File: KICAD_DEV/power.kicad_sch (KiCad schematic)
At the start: 16 parts, among them J1 USB_C_Receptacle_USB2.0_14P, J2 Screw_Terminal_01x02, U2 USBLC6-2SC6, U3 LMR33640ADDA

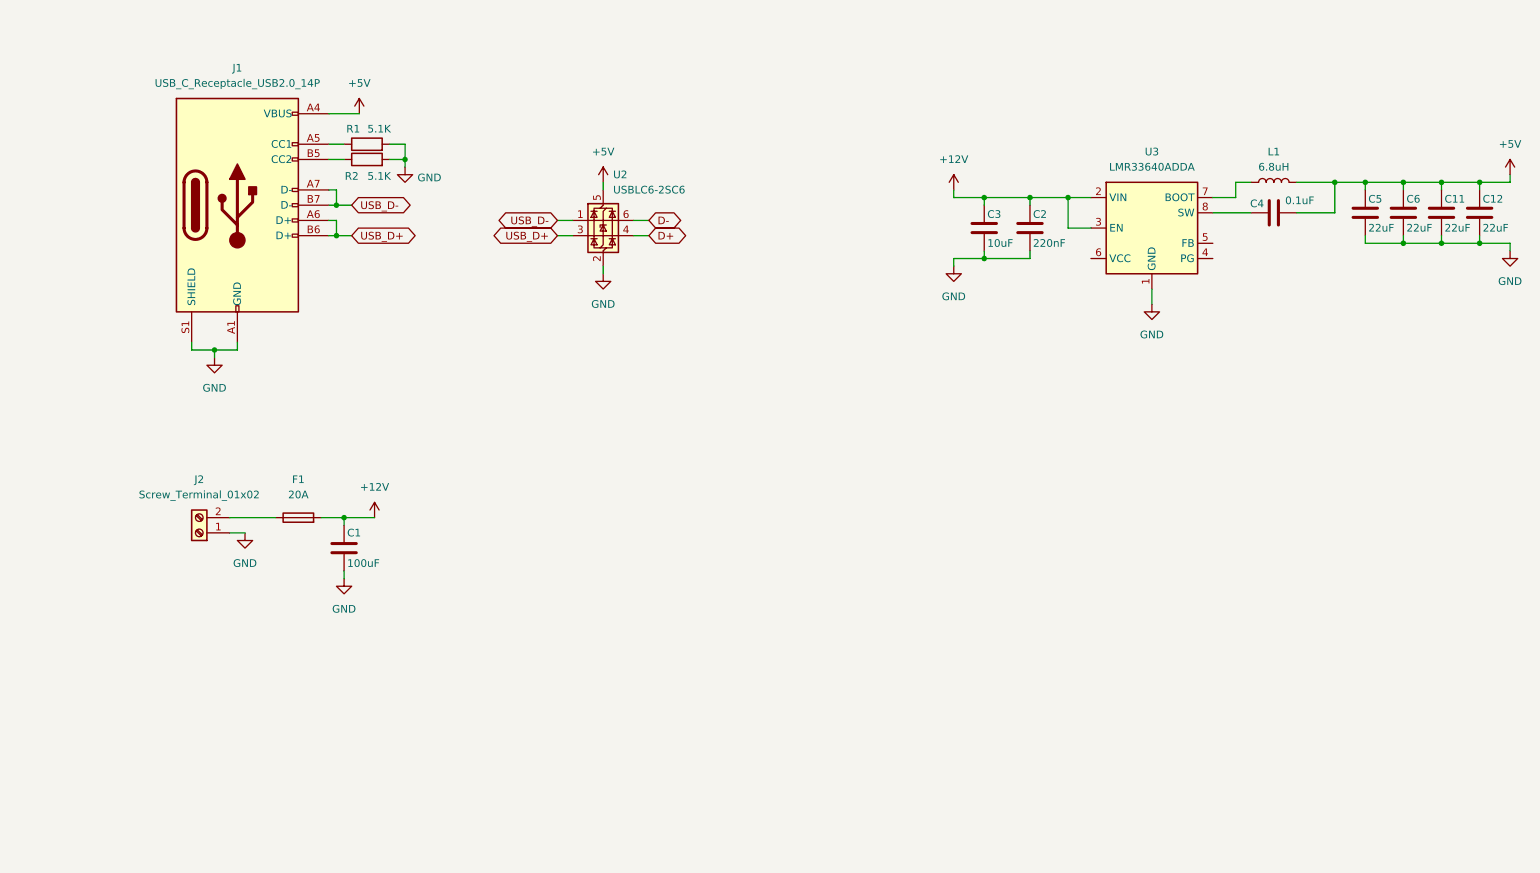
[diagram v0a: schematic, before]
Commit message: finished buck converter wiring!
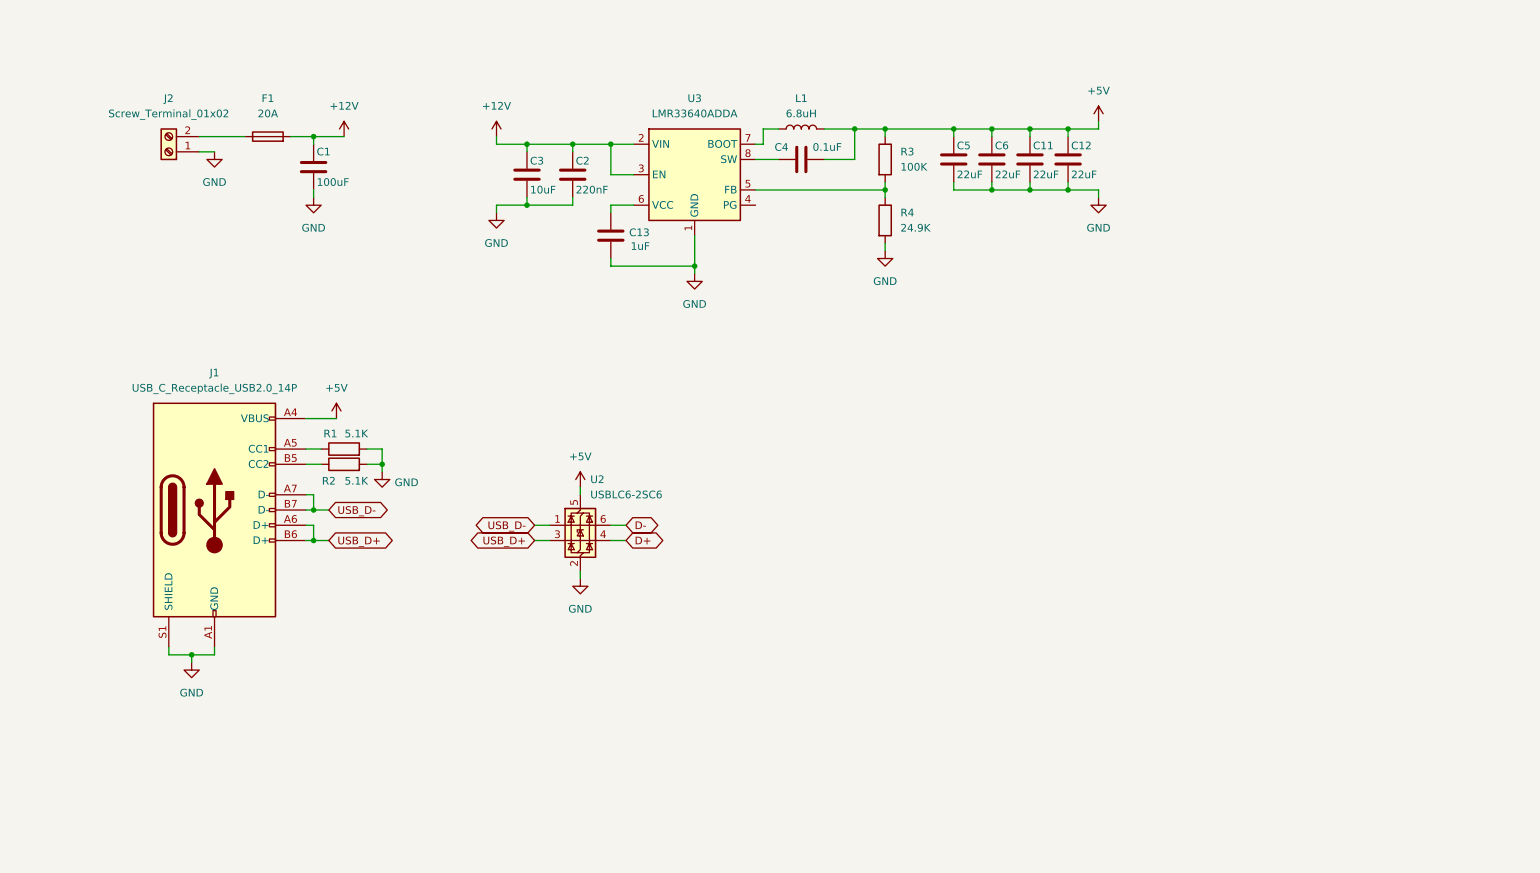
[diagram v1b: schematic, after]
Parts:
- added C13: 1uF, symbol Device:C
- added R3: 100K, symbol Device:R
- added R4: 24.9K, symbol Device:R
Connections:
- net +5V: now also R3.1
- net GND: now also C13.2, R4.2
- net at U3.5 (FB): now also R3.2, R4.1
- net at U3.6 (VCC): now also C13.1
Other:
- moved on the sheet: C1, C11, C12, C2, C3, C4, C5, C6, F1, J1, J2, L1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

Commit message: added all the basic footprints!
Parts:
- C11, C12, C5, C6: footprint (none) -> Capacitor_SMD:C_0805_2012Metric
- C13, C2, C4: footprint (none) -> Capacitor_SMD:C_0402_1005Metric
- C3: footprint (none) -> Capacitor_SMD:C_0603_1608Metric
- R1, R2, R3, R4: footprint (none) -> Resistor_SMD:R_0402_1005Metric
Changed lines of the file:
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@@
 			)
 		)
-		(property "Footprint" ""
+		(property "Footprint" "Resistor_SMD:R_0402_1005Metric"
 			(at 62.23 97.028 90)
 			(effects
@@
 			)
 		)
-		(property "Footprint" ""
+		(property "Footprint" "Capacitor_SMD:C_0805_2012Metric"
 			(at 177.4952 48.26 0)
 			(effects
@@
 			)
 		)
-		(property "Footprint" ""
+		(property "Footprint" "Capacitor_SMD:C_0805_2012Metric"
 			(at 164.7952 48.26 0)
 			(effects
@@
 			)
 		)
-		(property "Footprint" ""
+		(property "Footprint" "Capacitor_SMD:C_0402_1005Metric"
 			(at 142.24 43.4848 0)
 			(effects
@@
 			)
 		)
-		(property "Footprint" ""
+		(property "Footprint" "Capacitor_SMD:C_0805_2012Metric"
 			(at 171.1452 48.26 0)
 			(effects
@@
 			)
 		)
-		(property "Footprint" ""
+		(property "Footprint" "Capacitor_SMD:C_0805_2012Metric"
 			(at 183.8452 48.26 0)
 			(effects
@@
 			)
 		)
-		(property "Footprint" ""
+		(property "Footprint" "Capacitor_SMD:C_0402_1005Metric"
 			(at 107.6452 60.96 0)
 			(effects
@@
 			)
 		)
-		(property "Footprint" ""
+		(property "Footprint" "Capacitor_SMD:C_0603_1608Metric"
 			(at 93.6752 50.8 0)
 			(effects
@@
 			)
 		)
-		(property "Footprint" ""
+		(property "Footprint" "Resistor_SMD:R_0402_1005Metric"
 			(at 62.23 94.488 90)
 			(effects
@@
 			)
 		)
-		(property "Footprint" ""
+		(property "Footprint" "Capacitor_SMD:C_0402_1005Metric"
 			(at 101.2952 50.8 0)
 			(effects
@@
 			)
 		)
-		(property "Footprint" ""
+		(property "Footprint" "Resistor_SMD:R_0402_1005Metric"
 			(at 150.622 54.61 90)
 			(effects
@@
 			)
 		)
-		(property "Footprint" ""
+		(property "Footprint" "Resistor_SMD:R_0402_1005Metric"
 			(at 150.622 44.45 90)
 			(effects

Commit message: assigning more footprints!g
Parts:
- J2: footprint (none) -> TerminalBlock_Phoenix:TerminalBlock_Phoenix_PT-1,5-2-5.0-H_1x02_P5.00mm_Horizontal; Part (none) -> 1935776
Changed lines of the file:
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@@
 		(on_board yes)
 		(dnp no)
-		(fields_autoplaced yes)
 		(property "Reference" "J2"
-			(at 33.02 34.29 0)
+			(at 33.02 30.988 0)
 			(effects
 				(font
@@
 		)
 		(property "Value" "Screw_Terminal_01x02"
-			(at 33.02 36.83 0)
+			(at 33.02 33.528 0)
 			(effects
 				(font
@@
 			)
 		)
-		(property "Footprint" ""
+		(property "Footprint" "TerminalBlock_Phoenix:TerminalBlock_Phoenix_PT-1,5-2-5.0-H_1x02_P5.00mm_Horizontal"
 			(at 33.02 43.18 0)
 			(effects
@@
 			)
 		)
+		(property "Part" "1935776"
+			(at 33.02 36.322 0)
+			(effects
+				(font
+					(size 1.27 1.27)
+				)
+			)
+		)

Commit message: all footprints are in!
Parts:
- C1: footprint (none) -> Capacitor_SMD:C_Elec_8x6.2; Part (none) -> 25SVPF100M
- F1: footprint (none) -> Fuse:Fuse_Blade_Mini_directSolder
- J1: footprint (none) -> kai's library:USB_C_Receptacle_HRO_TYPE-C-31-M-12
- L1: footprint (none) -> Inductor_SMD:L_TechFuse_SL0650; Part (none) -> SMMS0650-6R8M
- U3: Current (none) -> 4A Continuous, 5A Max
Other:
- note added: "Probably change to fuse holder"
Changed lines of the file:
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@@
 	(generator_version "9.0")
 	(paper "A4")
+	(text "Probably change to fuse holder"
+		(exclude_from_sim no)
+		(at 50.546 26.67 0)
+		(effects
+			(font
+				(size 1.27 1.27)
+			)
+		)
+	)
 	(junction
 		(at 182.88 39.37)
@@
 			)
 		)
-		(property "Footprint" ""
+		(property "Footprint" "Fuse:Fuse_Blade_Mini_directSolder"
 			(at 49.53 42.418 90)
 			(effects
@@
 		(on_board yes)
 		(dnp no)
-		(fields_autoplaced yes)
 		(property "Reference" "L1"
-			(at 138.43 34.29 90)
+			(at 138.43 31.242 90)
 			(effects
 				(font
@@
 		)
 		(property "Value" "6.8uH"
-			(at 138.43 36.83 90)
-			(effects
-				(font
-					(size 1.27 1.27)
-				)
-			)
-		)
-		(property "Footprint" ""
+			(at 138.43 33.782 90)
+			(effects
+				(font
+					(size 1.27 1.27)
+				)
+			)
+		)
+		(property "Footprint" "Inductor_SMD:L_TechFuse_SL0650"
 			(at 138.43 39.37 0)
 			(effects
@@
 				)
 				(hide yes)
+			)
+		)
+		(property "Part" "SMMS0650-6R8M"
+			(at 138.43 36.322 90)
+			(effects
+				(font
+					(size 1.27 1.27)
+				)
 			)
 		)
@@
 		(dnp no)
 		(property "Reference" "C1"
-			(at 57.658 43.18 0)
+			(at 60.452 43.434 0)
 			(effects
 				(font
@@
 		)
 		(property "Value" "100uF"
-			(at 57.658 48.26 0)
+			(at 60.452 45.72 0)
 			(effects
 				(font
@@
 			)
 		)
-		(property "Footprint" ""
+		(property "Footprint" "Capacitor_SMD:C_Elec_8x6.2"
 			(at 58.1152 49.53 0)
 			(effects
@@
 				)
 				(hide yes)
+			)
+		)
+		(property "Part" "25SVPF100M"
+			(at 66.802 48.26 0)
+			(effects
+				(font
+					(size 1.27 1.27)
+				)
 			)
 		)
@@
 		(on_board yes)
 		(dnp no)
-		(fields_autoplaced yes)
 		(property "Reference" "U3"
 			(at 120.65 34.29 0)
@@
 				)
 				(hide yes)
+			)
+		)
+		(property "Current" "4A Continuous, 5A Max"
+			(at 120.65 27.432 0)
+			(effects
+				(font
+					(size 1.27 1.27)
+				)
 			)
 		)
@@
 			)
 		)
-		(property "Footprint" ""
+		(property "Footprint" "kai's library:USB_C_Receptacle_HRO_TYPE-C-31-M-12"
 			(at 44.45 102.87 0)
 			(effects

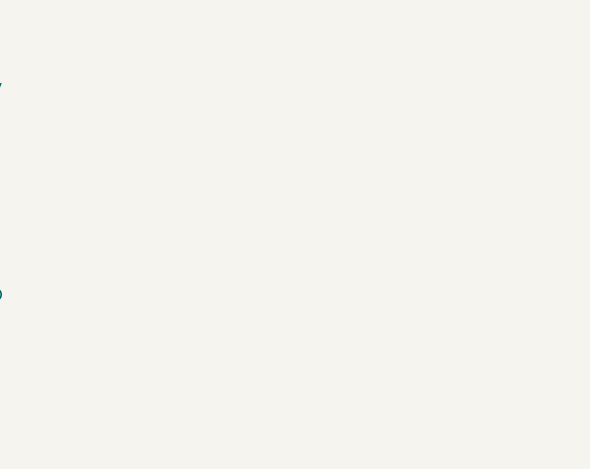
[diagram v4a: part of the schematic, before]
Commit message: added in the 1.5A 3V3 LDO!
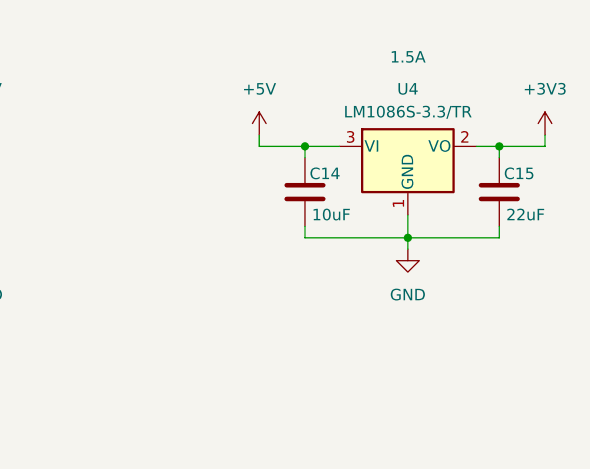
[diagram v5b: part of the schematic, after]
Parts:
- added C14: 10uF, symbol Device:C
- added C15: 22uF, symbol Device:C
- added U4: LM1086S-3.3/TR, Package_TO_SOT_SMD:TO-263-3_TabPin2, symbol Regulator_Linear:LM1084-3.3
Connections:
- net +5V: now also C14.1, U4.3 (VI)
- net GND: now also C14.2, C15.2, U4.1 (GND)
- new net +3V3: C15.1, U4.2 (VO)

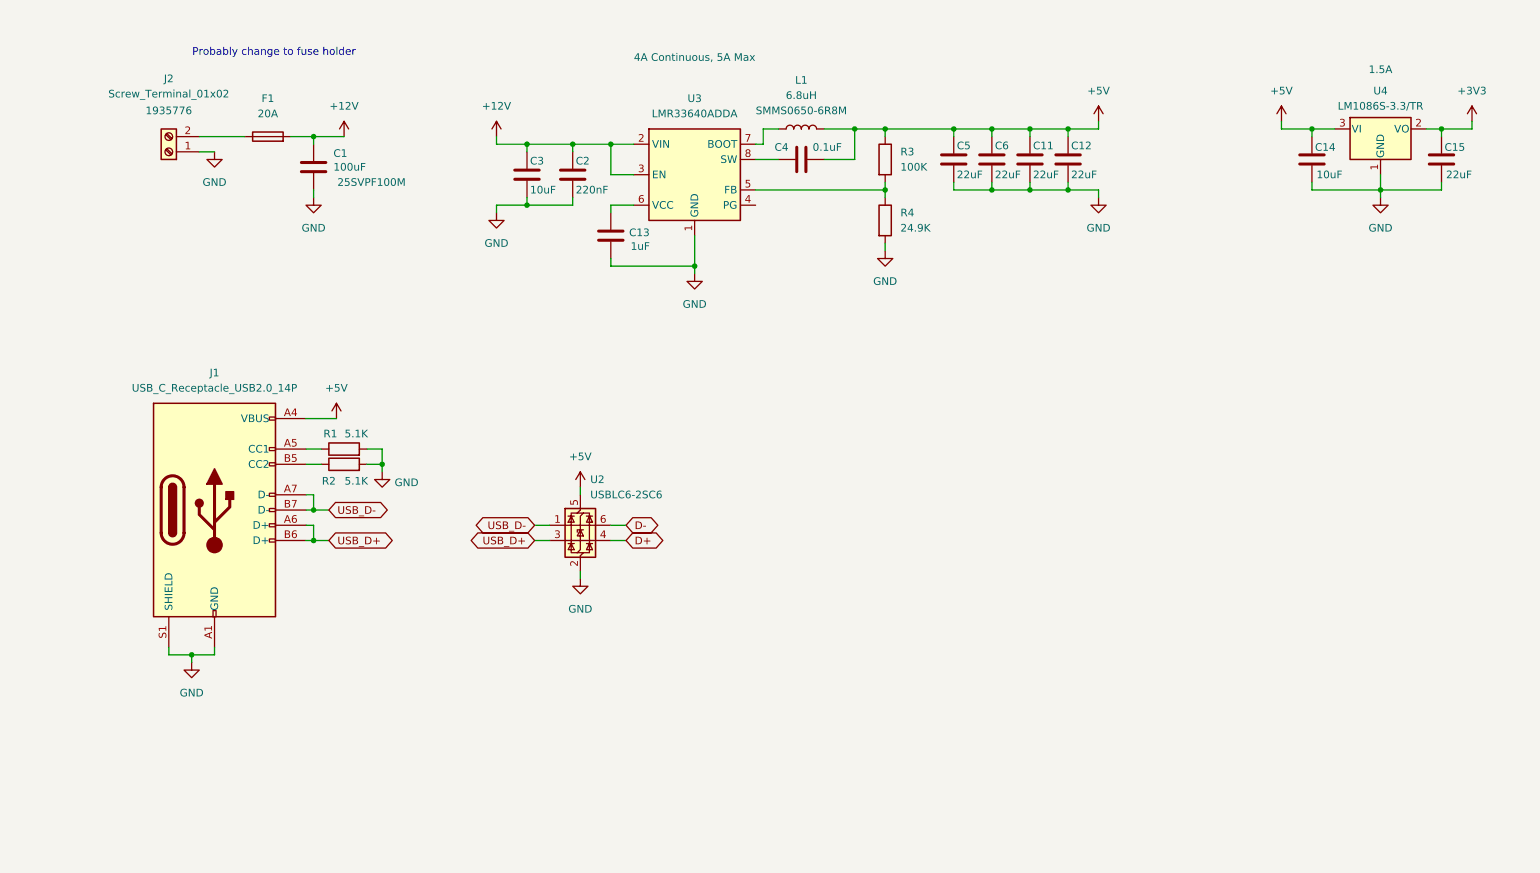
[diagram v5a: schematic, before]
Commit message: cleaning up the schematic, adding some footnotes for contributors!
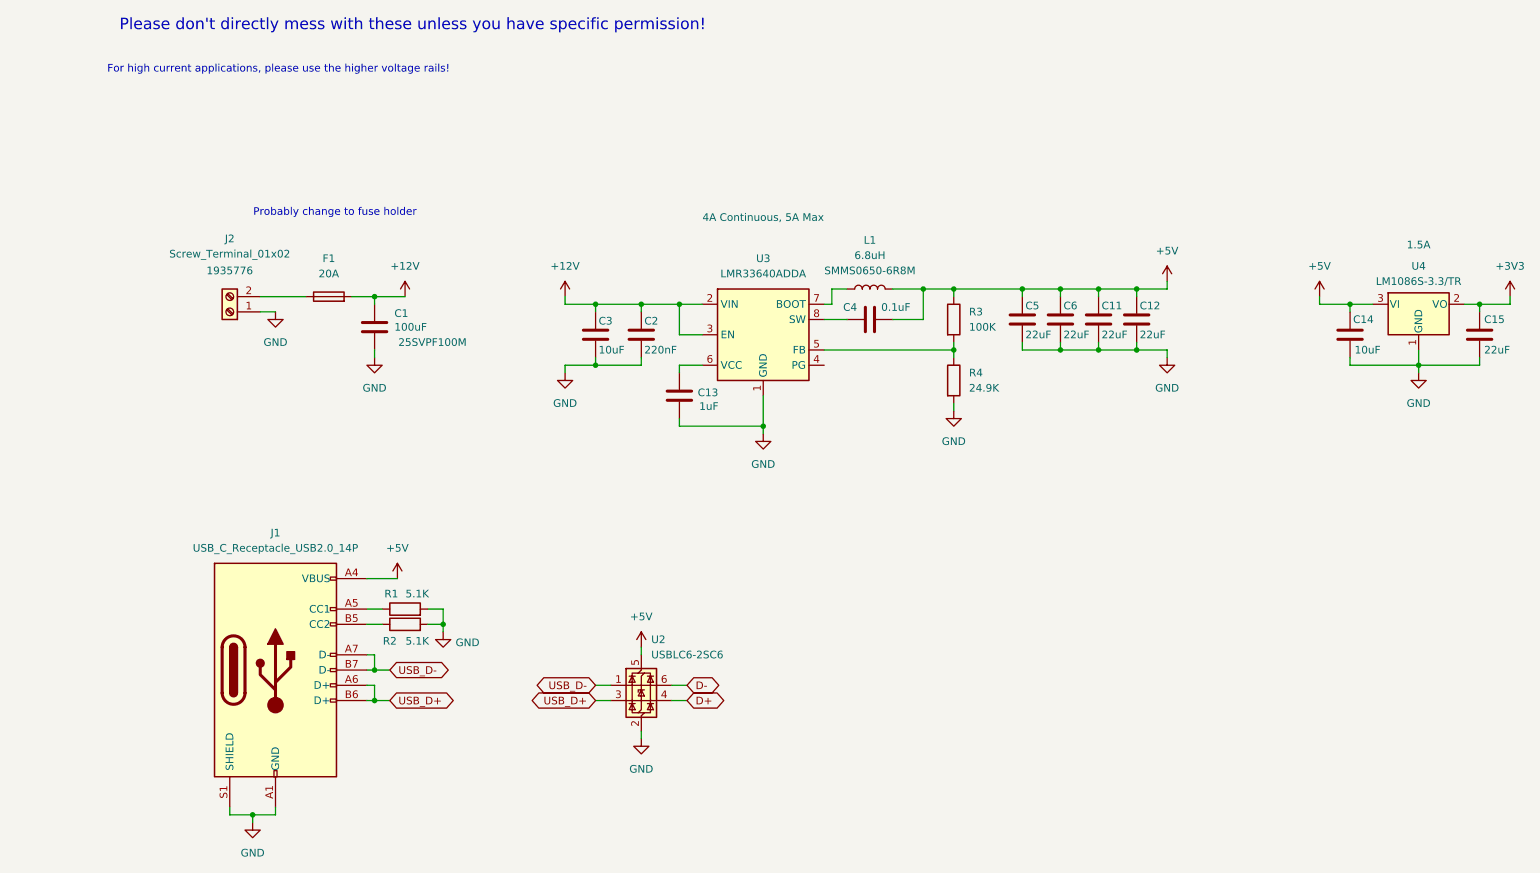
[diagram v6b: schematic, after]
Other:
- note added: "For high current applications, please use the higher voltage rails!"
- note added: "Please don't directly mess with these unless you have specific permission!"
- moved on the sheet: C1, C11, C12, C13, C14, C15, C2, C3, C4, C5, C6, F1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

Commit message: starting the actual board!
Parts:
- C14, C15: footprint (none) -> Capacitor_SMD:C_0805_2012Metric
- F1: footprint Fuse:Fuse_Blade_Mini_directSolder -> Fuse:FuseHolder_Blade_ATO_Littelfuse_FLR_178.6165
- J1: footprint kai's library:USB_C_Receptacle_HRO_TYPE-C-31-M-12 -> Connector_USB:USB_C_Receptacle_HRO_TYPE-C-31-M-12
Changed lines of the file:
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@@
 			)
 		)
-		(property "Footprint" ""
+		(property "Footprint" "Capacitor_SMD:C_0805_2012Metric"
 			(at 230.8352 77.47 0)
 			(effects
@@
 			)
 		)
-		(property "Footprint" ""
+		(property "Footprint" "Capacitor_SMD:C_0805_2012Metric"
 			(at 252.4252 77.47 0)
 			(effects
@@
 			)
 		)
-		(property "Footprint" "Fuse:Fuse_Blade_Mini_directSolder"
+		(property "Footprint" "Fuse:FuseHolder_Blade_ATO_Littelfuse_FLR_178.6165"
 			(at 59.69 69.088 90)
 			(effects
@@
 			)
 		)
-		(property "Footprint" "kai's library:USB_C_Receptacle_HRO_TYPE-C-31-M-12"
+		(property "Footprint" "Connector_USB:USB_C_Receptacle_HRO_TYPE-C-31-M-12"
 			(at 54.61 129.54 0)
 			(effects

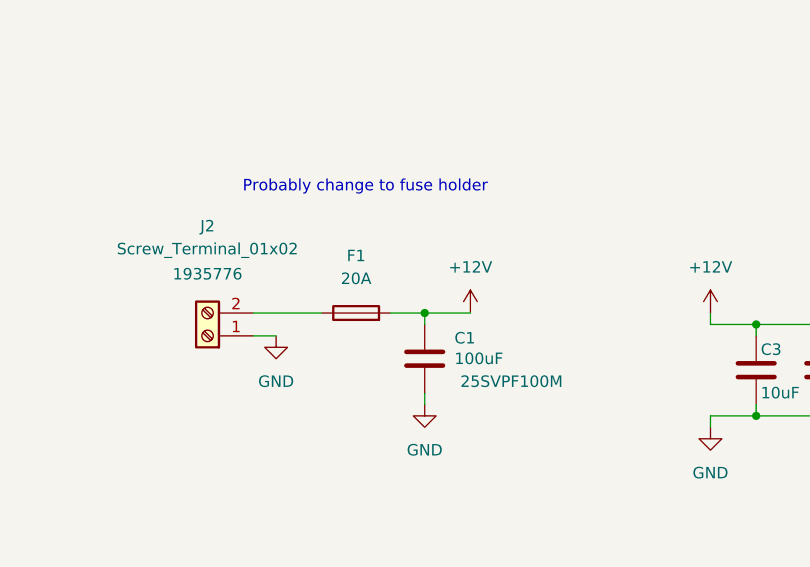
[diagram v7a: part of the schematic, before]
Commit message: changing cap size, but it's probably not adequate
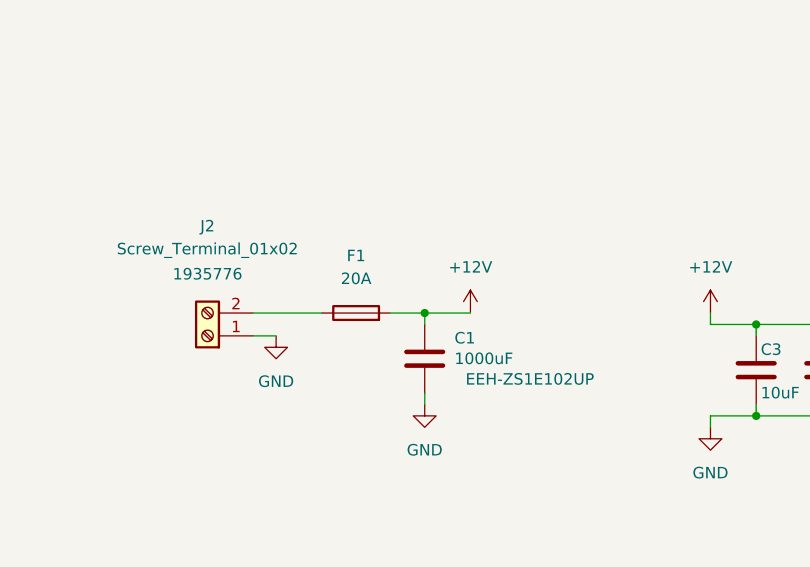
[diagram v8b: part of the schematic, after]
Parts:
- C1: value 100uF -> 1000uF; footprint Capacitor_SMD:C_Elec_8x6.2 -> Capacitor_SMD:C_Elec_10x10.2; Part 25SVPF100M -> EEH-ZS1E102UP
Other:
- note removed: "Probably change to fuse holder"
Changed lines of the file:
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@@
 		)
 	)
-	(text "Probably change to fuse holder"
-		(exclude_from_sim no)
-		(at 60.706 53.34 0)
-		(effects
-			(font
-				(size 1.27 1.27)
-			)
-		)
-	)
 	(text "For high current applications, please use the higher voltage rails!"
 		(exclude_from_sim no)
@@
 			)
 		)
-		(property "Value" "100uF"
+		(property "Value" "1000uF"
 			(at 70.612 72.39 0)
 			(effects
@@
 			)
 		)
-		(property "Footprint" "Capacitor_SMD:C_Elec_8x6.2"
+		(property "Footprint" "Capacitor_SMD:C_Elec_10x10.2"
 			(at 68.2752 76.2 0)
 			(effects
@@
 			)
 		)
-		(property "Part" "25SVPF100M"
-			(at 76.962 74.93 0)
+		(property "Part" "EEH-ZS1E102UP"
+			(at 78.994 74.676 0)
 			(effects
 				(font
